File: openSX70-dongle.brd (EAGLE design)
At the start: 47.8 x 24.3 mm, 22 parts, among them J1 AUDIO_JACK_3.5MM_PTH

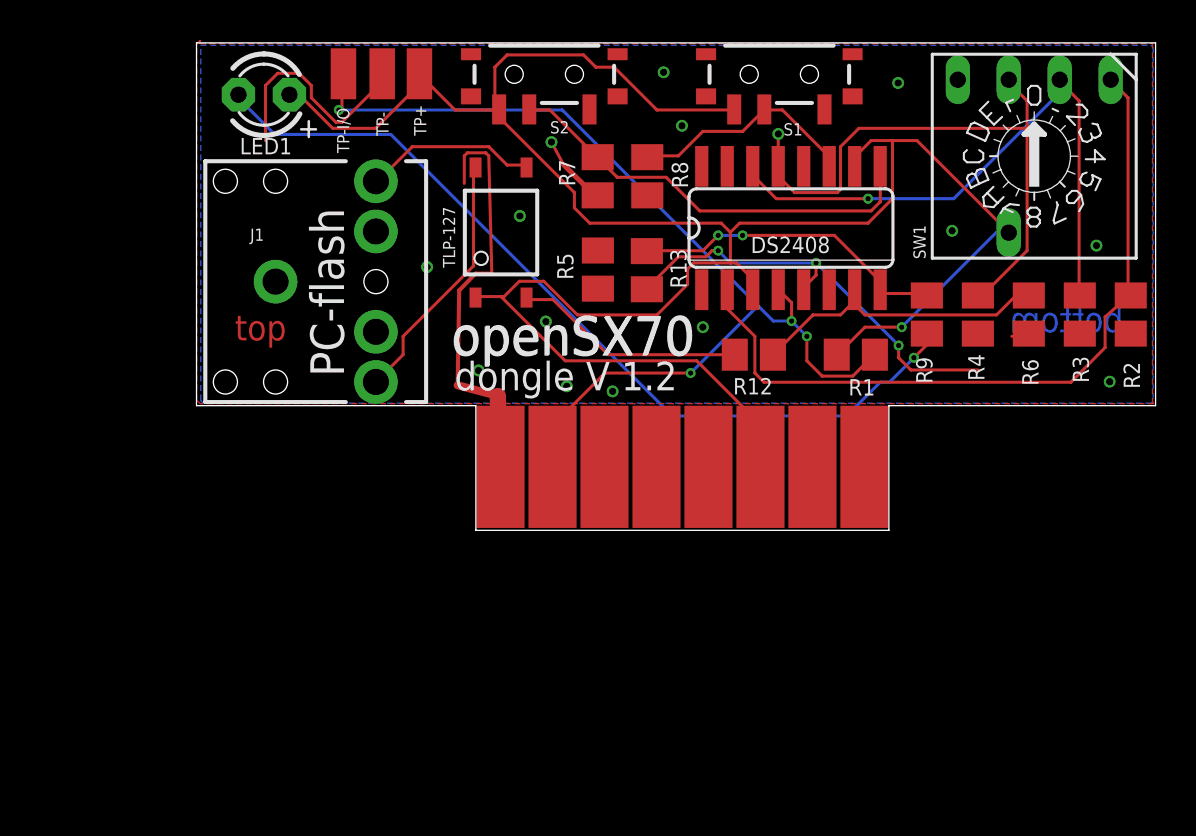
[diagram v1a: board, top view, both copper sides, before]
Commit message: version 2.0 dongle
EagleCAD version 2.0 dongle
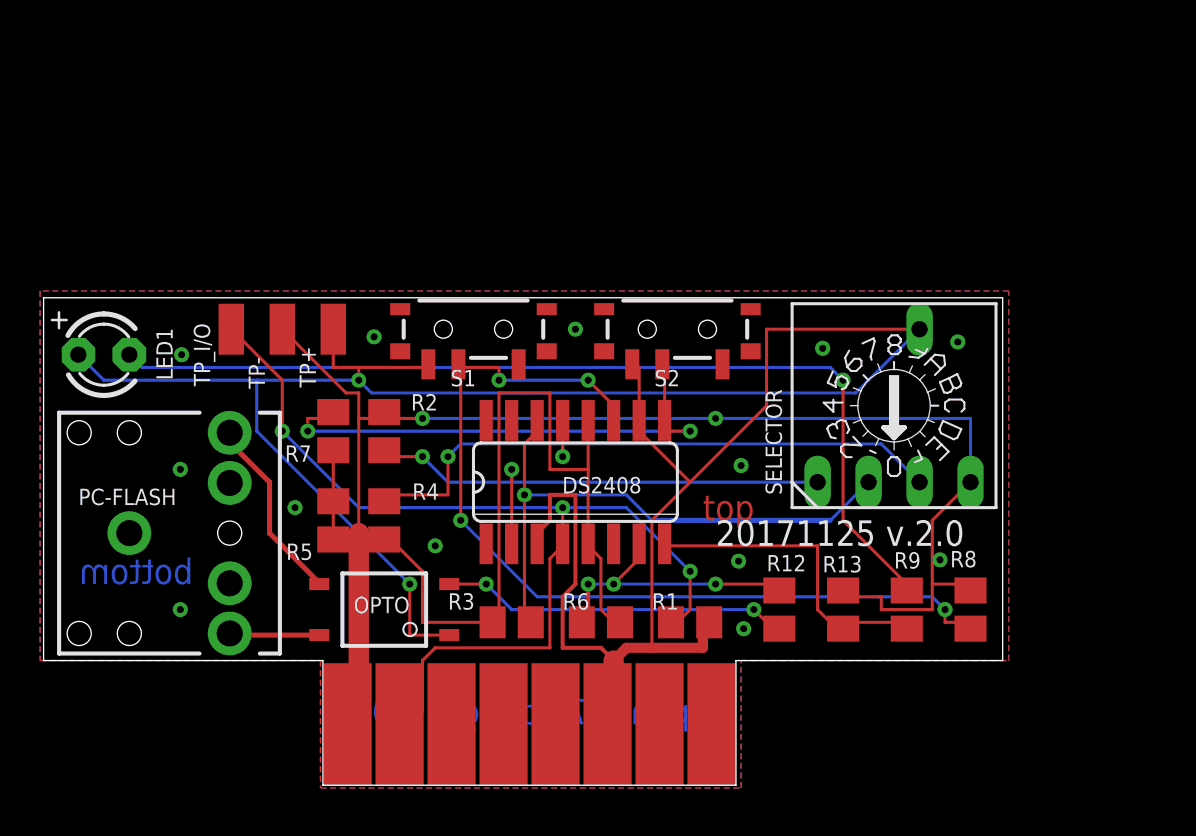
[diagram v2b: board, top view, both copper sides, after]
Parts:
- removed J1: AUDIO_JACK_3.5MM_PTH, SparkFun-Connectors:AUDIO-JACK
- removed SW1: (no value), special:SW-C16
- removed TLP-127: TLP127, openSX70:SO-4
- removed TP-I/O: (no value), wirepad:SMD1,27-2,54
- added OPTO: TLP127, openSX70:SO-4
- added PC-FLASH: AUDIO_JACK_3.5MM_PTH, SparkFun-Connectors:AUDIO-JACK
- added SELECTOR: (no value), special:SW-C16
- added TP_I/O: (no value), wirepad:SMD1,27-2,54
- moved R2 37.6 mm to (18.4, 19.1), turned to 90 degrees
- moved R3 32.2 mm to (24.8, 9.53), turned to 0 degrees
- moved R4 31.3 mm to (18.4, 14.6)
- moved R8 26.9 mm to (47.6, 10.2), turned to 90 degrees
- moved R6 26.3 mm to (29.2, 9.53), turned to 0 degrees
- moved S1 19.8 mm to (22.9, 24.1)
- moved R13 19.5 mm to (41.3, 10.2), turned to 90 degrees
- moved R7 18.3 mm to (15.9, 19.1)
- moved R5 18.2 mm to (15.9, 14.6), turned to 270 degrees
- moved DS2408 16.6 mm to (27.9, 16.5)
- moved R1 15.7 mm to (33.7, 9.53), turned to 0 degrees
- moved LED1 15.2 mm to (4.45, 22.9), turned to 0 degrees
- moved U$1 14.9 mm to (25.7, 4.45)
- moved R9 14.7 mm to (44.5, 10.2), turned to 90 degrees
- moved S2 14.3 mm to (33.0, 24.1)
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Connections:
- removed net GND-ISO: DS2408.12, DS2408.13, DS2408.5, R13.2, R2.2, R3.1, R4.1, R4.2, R5.1, R5.2, R6.2, R7.2, SW1.4, SW1.8, U$1.P$1
- new net GND: DS2408.12, DS2408.5, R13.2, R2.2, R3.1, R4.1, R5.1, R5.2, R6.2, R7.2, R8.2, SELECTOR.8, TP-.1, U$1.P$1
- net N$1: now also TP_I/O.1; no longer TP-I/O.1
- net N$10: now also OPTO.2; no longer TLP-127.2
- net N$12: now also OPTO.4, PC-FLASH.TIP; no longer J1.TIP, TLP-127.4
- net N$15: now also OPTO.3, PC-FLASH.RING; no longer J1.RING, TLP-127.3
- net N$3: now also SELECTOR.1; no longer SW1.1
- net N$4: now also SELECTOR.2; no longer SW1.2
- net N$5: now also DS2408.13, R4.2, SELECTOR.4; no longer TP-.1
- net VCC: now also OPTO.1, SELECTOR.C; no longer SW1.C, TLP-127.1
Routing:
- net GND: track 0.00 -> 117.8 mm, vias 0 -> 15
- net GND-ISO: track 77.9 -> 0.00 mm, vias 18 -> 0
- net N$6: track 11.5 -> 45.5 mm, vias 0 -> 4
- net N$5: track 11.4 -> 32.4 mm, vias 0 -> 2
- net VCC: track 113.6 -> 126.6 mm, vias 1 -> 2
- net N$3: track 37.5 -> 26.8 mm, vias 0 -> 2
- net N$12: track 12.8 -> 4.56 mm
- net N$10: track 11.6 -> 17.9 mm, vias 0 -> 2
- net N$2: track 43.1 -> 47.9 mm
- net N$7: track 21.5 -> 25.9 mm, vias 0 -> 2
- net N$1: track 51.8 -> 50.3 mm, vias 4 -> 3
- net N$11: track 15.8 -> 14.6 mm, vias 0 -> 3
- net N$4: track 30.2 -> 29.1 mm
- net N$8: track 15.8 -> 16.8 mm, vias 2 -> 0
- net N$15: track 8.67 -> 9.45 mm
- added copper zone on layer 1, net GND
- added copper zone on layer 16, net GND
- removed copper zone on layer 1, net GND-ISO
- removed copper zone on layer 16, net GND-ISO
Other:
- board text added: "20171125 v.2.0"
- board text added: "openSX70 dongle 2.0"
- board text removed: "PC-flash"
- board text removed: "dongle V 1.2"
- board text removed: "openSX70"

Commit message: Proper upload of version 2.1 openSX70 dongle
Version 2.1 manufactured by EasyEDA
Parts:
- moved R3 10.3 mm to (21.0, 19.1), turned to 90 degrees
- moved R6 3.24 mm to (26.0, 10.2)
- moved R1 2.62 mm to (31.1, 10.2), turned to 180 degrees
- moved DS2408 1.27 mm to (29.2, 16.5)
- turned SELECTOR to 180 degrees
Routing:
- net GND: track 117.8 -> 0.00 mm, vias 15 -> 13
- net VCC: track 126.6 -> 80.4 mm
- net N$3: track 26.8 -> 41.7 mm
- net N$1: track 50.3 -> 43.3 mm, vias 3 -> 2
- net N$6: track 45.5 -> 39.2 mm, vias 4 -> 2
- net N$2: track 47.9 -> 43.9 mm
- net N$5: track 32.4 -> 36.3 mm
- net N$7: track 25.9 -> 29.8 mm
- net N$8: track 16.8 -> 14.3 mm
- net N$11: track 14.6 -> 16.1 mm, vias 3 -> 2
- net N$4: track 29.1 -> 29.8 mm
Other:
- board size 47.8 x 24.3 mm -> 47.8 x 24.4 mm
- board text added: "20171125 v.2.1"
- board text added: "openSX70 dongle 2.1"
- board text removed: "20171125 v.2.0"
- board text removed: "openSX70 dongle 2.0"

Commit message: Moved to 2.2 there was a ground loose on the DS2408!!!
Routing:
- net GND: track 0.00 -> 2.09 mm, vias 13 -> 14
- net N$4: track 29.8 -> 30.6 mm
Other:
- board text added: "20171212 v.2.2"
- board text removed: "20171125 v.2.1"

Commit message: Fix big flaws. Selector pin 8 was not connected to P3 (pin 12) D'ho!!
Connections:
- new net N$13: DS2408.12, R5.2, SELECTOR.8
- net GND: no longer DS2408.12, R5.2, SELECTOR.8
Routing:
- net N$13: track 0.00 -> 45.5 mm, vias 0 -> 3
- net N$5: track 36.3 -> 39.9 mm
- net GND: track 2.09 -> 0.00 mm, vias 14 -> 16
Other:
- board text added: "20171222 v.2.3"
- board text removed: "20171212 v.2.2"

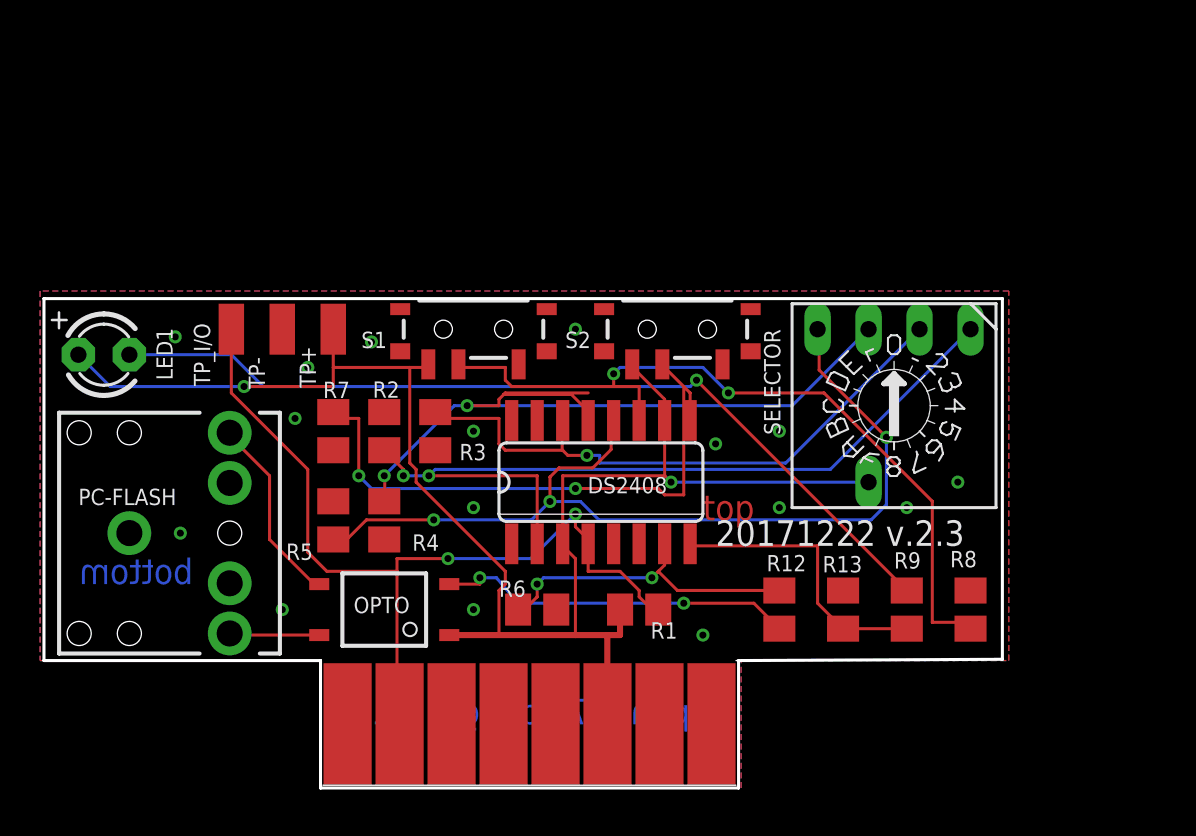
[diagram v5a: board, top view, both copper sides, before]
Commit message: P7 and P6 had a pulldown resistor when a pullup was needed. More D'ho! stuff.
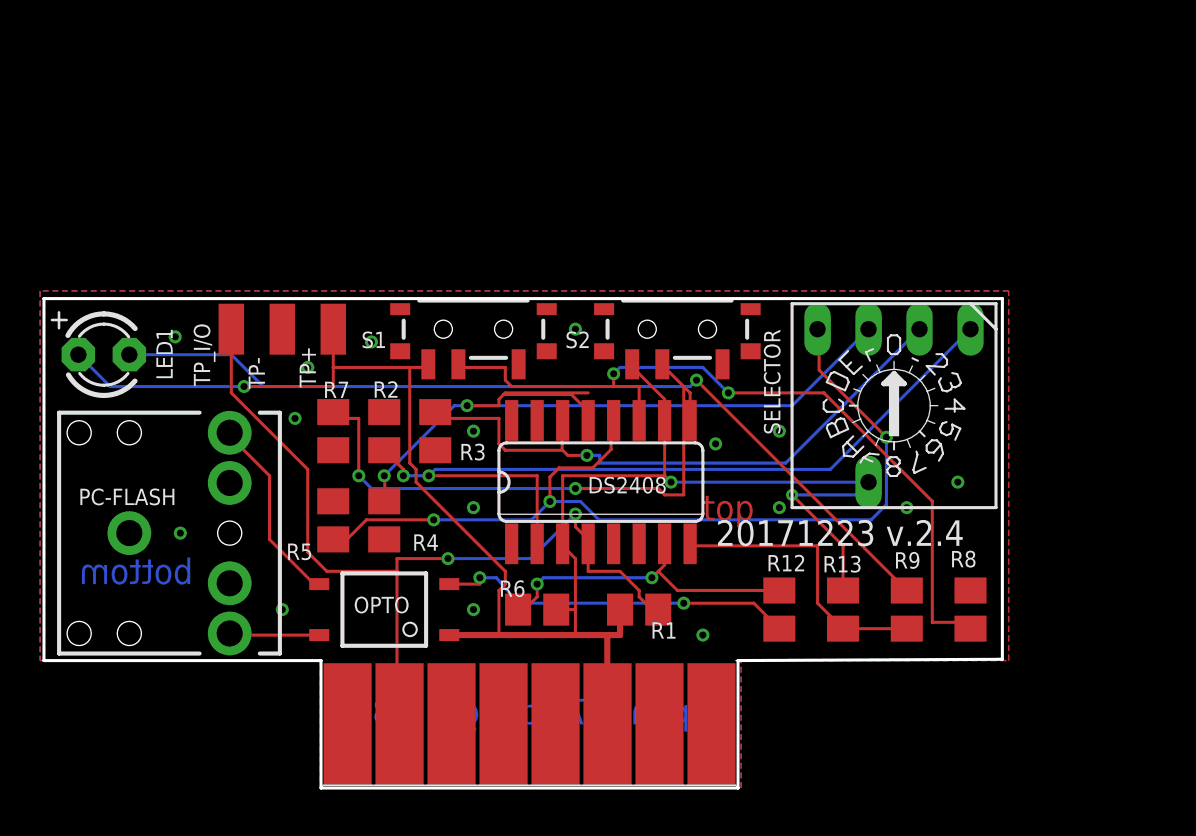
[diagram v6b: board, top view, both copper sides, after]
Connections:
- net GND: no longer R13.2, R6.2
- net VCC: now also R13.2, R6.2
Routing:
- net VCC: track 80.4 -> 91.3 mm, vias 2 -> 3
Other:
- board text added: "20171223 v.2.4"
- board text added: "openSX70 dongle 2.3"
- board text removed: "20171222 v.2.3"
- board text removed: "openSX70 dongle 2.1"

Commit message: Had all the connections on the BCD wrong, now P0->pin2 DS->pin8 BCD P1->pin14 DS->pin4 BCD P2->pin13 DS->pin2 BCD P3->pin12 DS->pin1 BCD (same as in prototype). Also made the flash connector longer to allow for a case. Gone to version 2.6
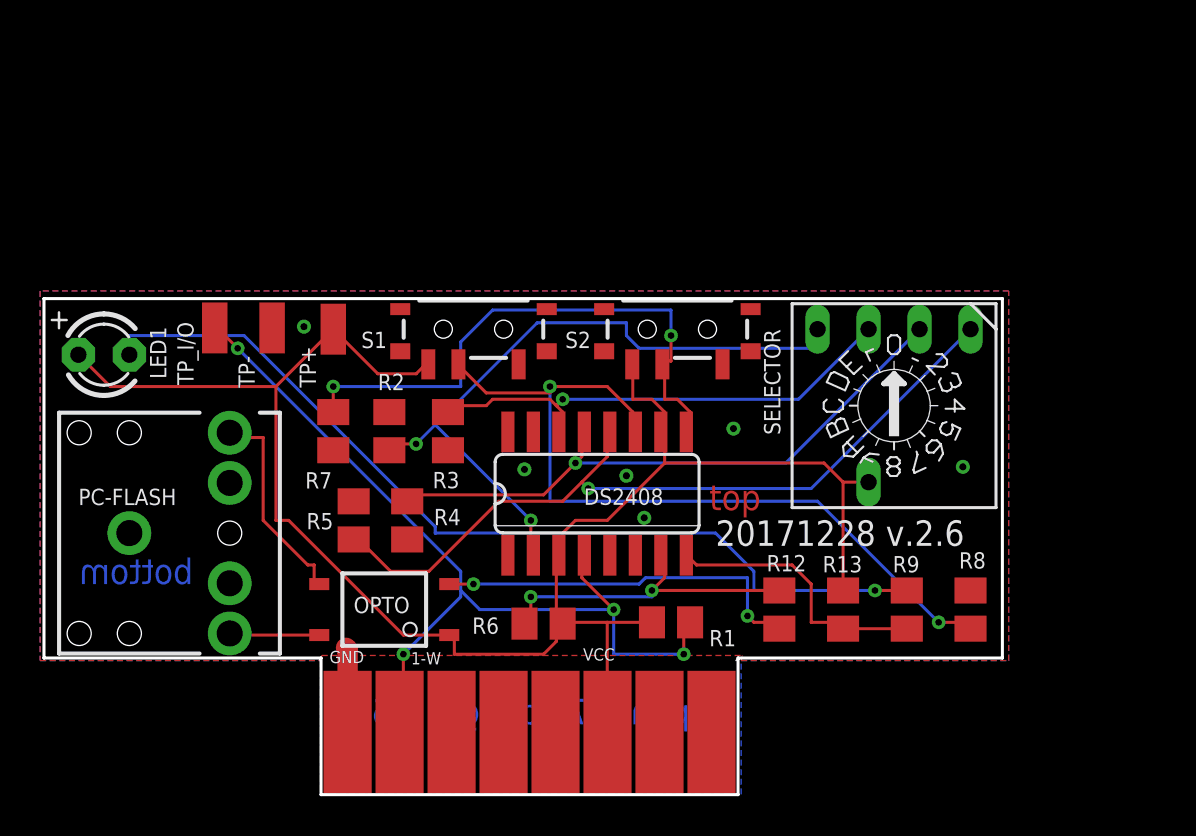
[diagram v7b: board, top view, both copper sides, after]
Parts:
- moved R1 1.71 mm to (32.7, 9.53)
- moved R4 1.14 mm to (19.6, 14.6)
- moved R5 1.02 mm to (16.9, 14.6)
- moved TP_I/O 0.83 mm to (9.97, 24.2)
- moved R6 0.77 mm to (26.4, 9.46)
- moved R3 0.64 mm to (21.6, 19.1)
- moved DS2408 0.60 mm to (29.0, 15.9)
- moved TP- 0.51 mm to (12.8, 24.2)
- moved U$1 0.38 mm to (25.7, 4.06)
- moved R2 0.25 mm to (18.7, 19.1)
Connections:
- net N$13: now also SELECTOR.1; no longer SELECTOR.8
- net N$3: now also SELECTOR.8; no longer SELECTOR.1
- net N$4: now also SELECTOR.4; no longer SELECTOR.2
- net N$5: now also SELECTOR.2; no longer SELECTOR.4
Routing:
- net N$5: track 39.9 -> 30.8 mm, vias 2 -> 1
- net N$3: track 41.7 -> 34.5 mm
- net N$4: track 30.7 -> 24.5 mm
- net N$13: track 45.5 -> 39.7 mm, vias 3 -> 1
- net GND: track 0.00 -> 4.22 mm, vias 16 -> 6
- net N$1: track 43.3 -> 45.6 mm, vias 2 -> 4
- net VCC: track 91.3 -> 89.3 mm, vias 3 -> 0
- net N$2: track 43.9 -> 45.7 mm
- net N$6: track 39.2 -> 40.8 mm
- net N$7: track 29.8 -> 28.5 mm
- net N$15: track 9.52 -> 10.6 mm
- net N$10: track 17.9 -> 18.9 mm
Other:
- board size 47.8 x 24.4 mm -> 47.8 x 24.7 mm
- board text added: "1-W"
- board text added: "20171228 v.2.6"
- board text added: "GND"
- board text added: "VCC"
- board text added: "openSX70 dongle 2.6"
- board text removed: "20171223 v.2.4"
- board text removed: "openSX70 dongle 2.3"
